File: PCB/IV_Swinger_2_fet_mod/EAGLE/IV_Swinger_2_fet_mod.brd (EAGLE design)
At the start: 59.7 x 53.3 mm, 33 parts, among them J1 

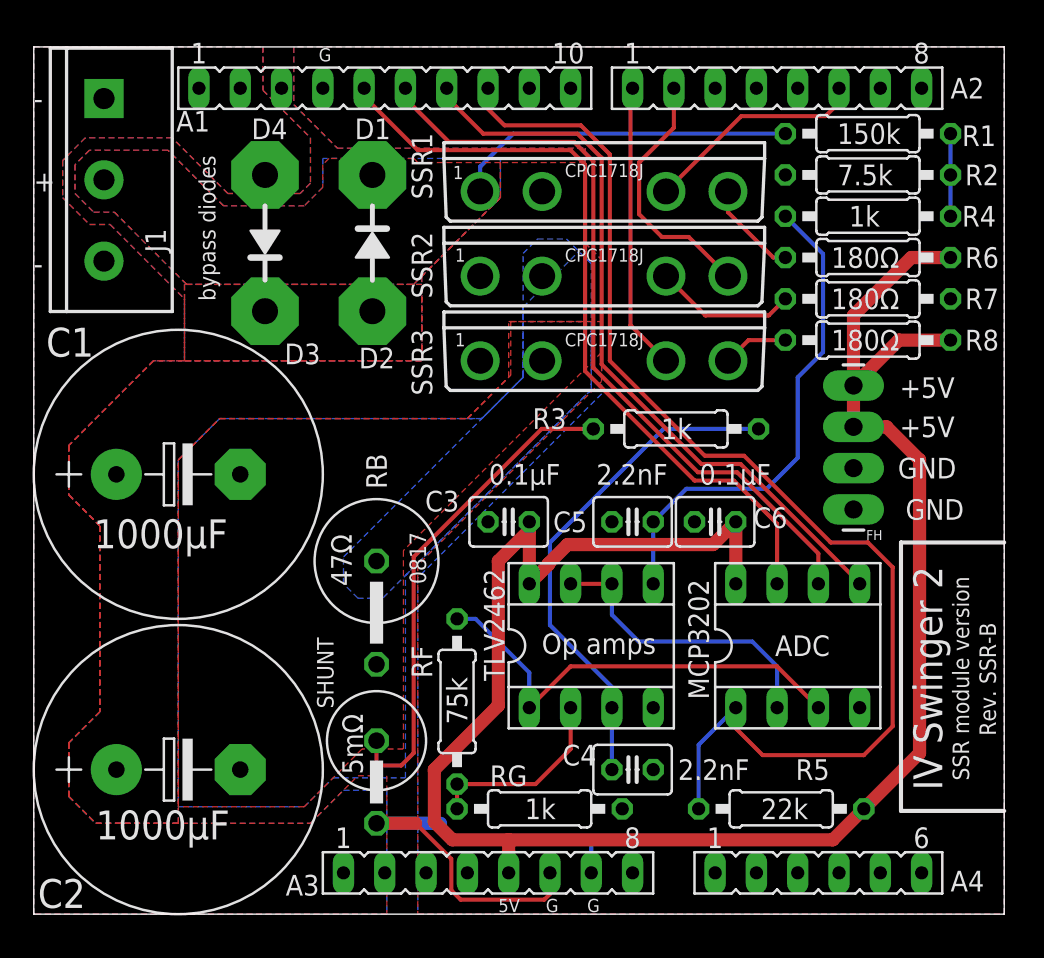
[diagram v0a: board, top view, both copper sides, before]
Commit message: Correct EAGLE files for FET module version (Issue #218)
Replace the incorrect files with the correct ones.
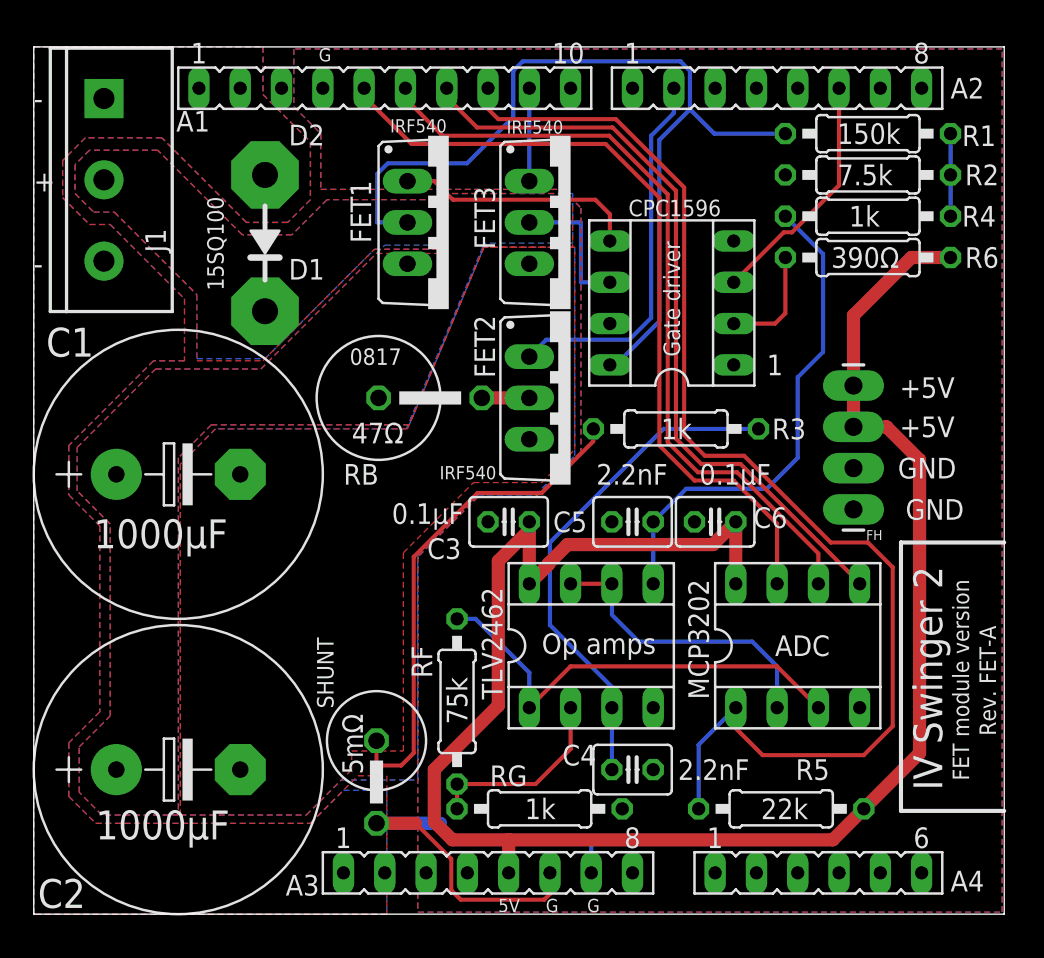
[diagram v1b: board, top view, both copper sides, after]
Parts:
- removed D3, D4: WIREPAD4,16O1,6, wirepad:4,16O1,6
- removed R7, R8: 180Ω, rcl:0207/10
- removed SSR1, SSR2, SSR3: CPC1718J, my_relay:I4-PAC
- added CPC1596: Gate driver, ic-package:SOCKET-08
- added FET1, FET2, FET3: IRF540, transistor-power:TO220BV
- R6: value 180Ω -> 390Ω
- moved RB 16.0 mm to (26.3, 31.8), turned to 0 degrees
- moved D1 10.7 mm to (14.2, 37.1)
- moved D2 10.7 mm to (14.2, 45.5)
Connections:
- removed net BLEED+: RB.1, SSR2.2
- removed net N10: R8.1, SSR3.4
- removed net N15: D2.1, D3.1
- removed net N8: R6.1, SSR1.4
- removed net N9: R7.1, SSR2.3
- new net N$2: FET2.D, RB.2
- new net N$3: CPC1596.5, FET1.G
- new net N$4: CPC1596.2, R6.1
- net +5V: no longer R8.2
- net GND: now also D2.1; no longer D4.1, R7.2
- net LOAD_CAP+: now also CPC1596.6, FET1.S, FET3.D, RB.1; no longer SSR1.2, SSR2.1, SSR3.1
- net LOAD_CAP-: now also FET2.S, FET3.S; no longer RB.2, SSR3.2
- net N1: now also CPC1596.3; no longer SSR1.3
- net N2: now also FET2.G; no longer SSR2.4
- net N3: now also A1.9, FET3.G; no longer A2.1, SSR3.3
- net PV+: now also CPC1596.8, FET1.D; no longer SSR1.1
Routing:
- net PV+: track 21.1 -> 55.7 mm
- net N$3: track 0.00 -> 14.9 mm
- net N3: track 17.7 -> 5.71 mm
- net N9: track 8.77 -> 0.00 mm
- net LOAD_CAP+: track 0.00 -> 8.64 mm
- net N2: track 15.7 -> 23.2 mm
- net +5V: track 121.7 -> 114.6 mm
- net N$4: track 0.00 -> 6.87 mm
- net N8: track 5.96 -> 0.00 mm
- net N10: track 4.06 -> 0.00 mm
- net N$2: track 0.00 -> 2.92 mm
- net N6: track 46.9 -> 48.4 mm
- net N7: track 47.9 -> 49.4 mm
- net N5: track 45.8 -> 47.3 mm
- net N4: track 74.6 -> 76.1 mm
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- removed copper zone on layer 16, net BLEED+
- removed copper zone on layer 1, net N15
- removed copper zone on layer 16, net N15
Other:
- board text added: "15SQ100"
- board text added: "390Ω"
- board text added: "FET module version"
- board text added: "Rev. FET-A"
- board text removed: "180Ω"
- board text removed: "Rev. SSR-B"
- board text removed: "SSR module version"
- board text removed: "bypass diodes"
